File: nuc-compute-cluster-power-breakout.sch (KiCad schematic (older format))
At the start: 20 parts, among them J10 10107844-002LF, J2 BM04B-SRSS-TB-LF-SN, J3 BM04B-SRSS-TB-LF-SN, J5 430450812, J6 430450812, J7 430450812, J8 430450812, J9 430450812, Q11 BC856,215

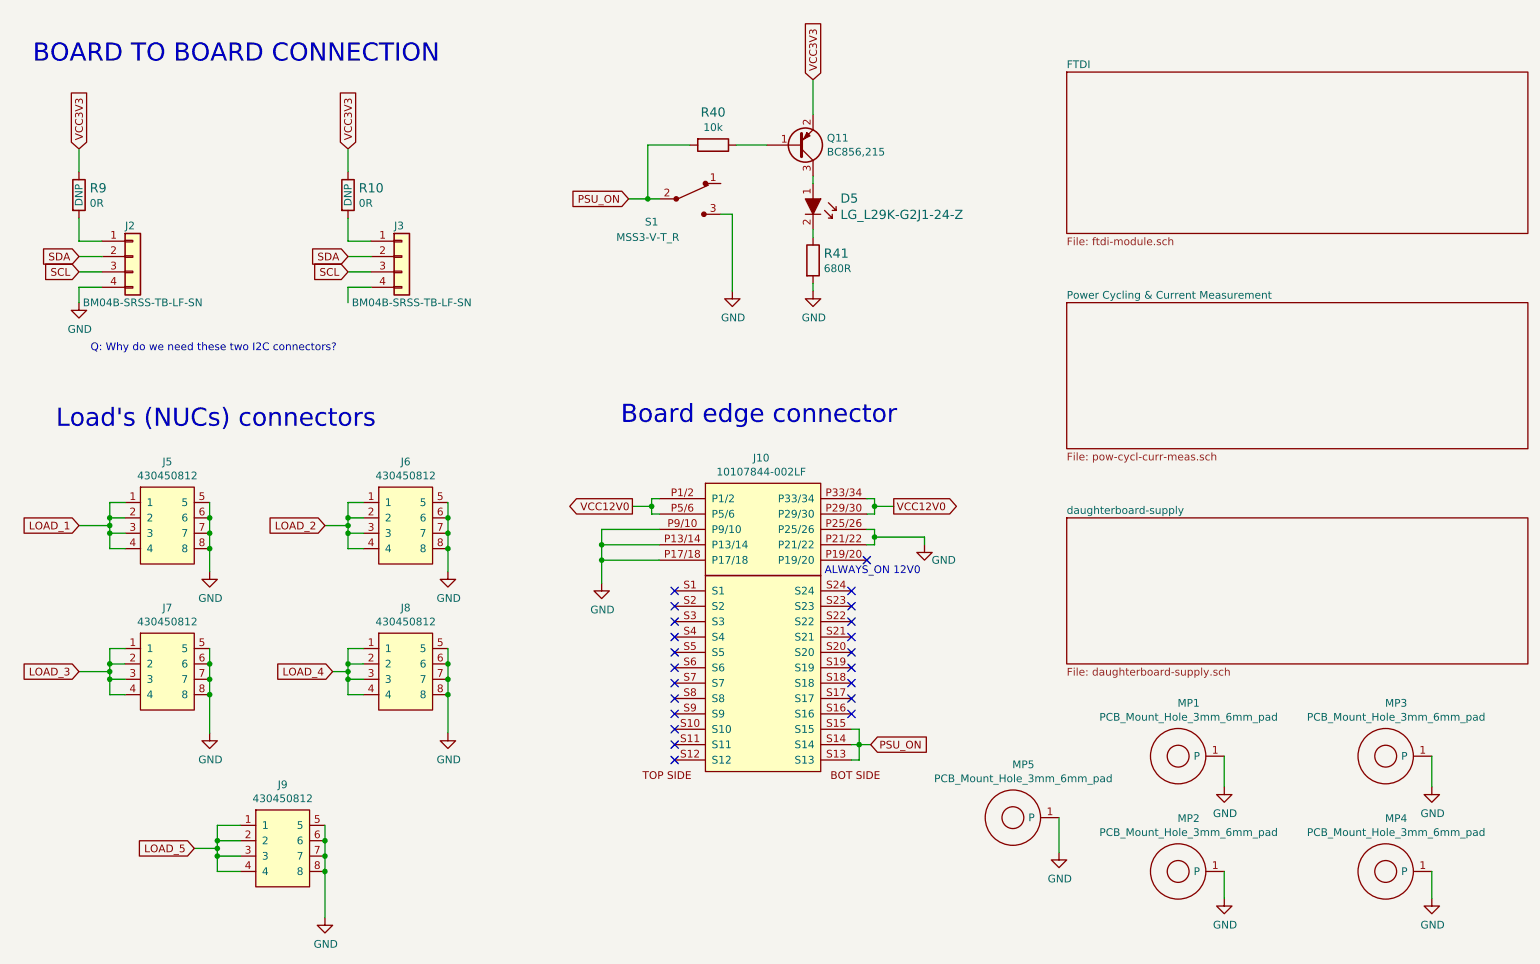
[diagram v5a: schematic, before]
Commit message: Add remarks to the schematic
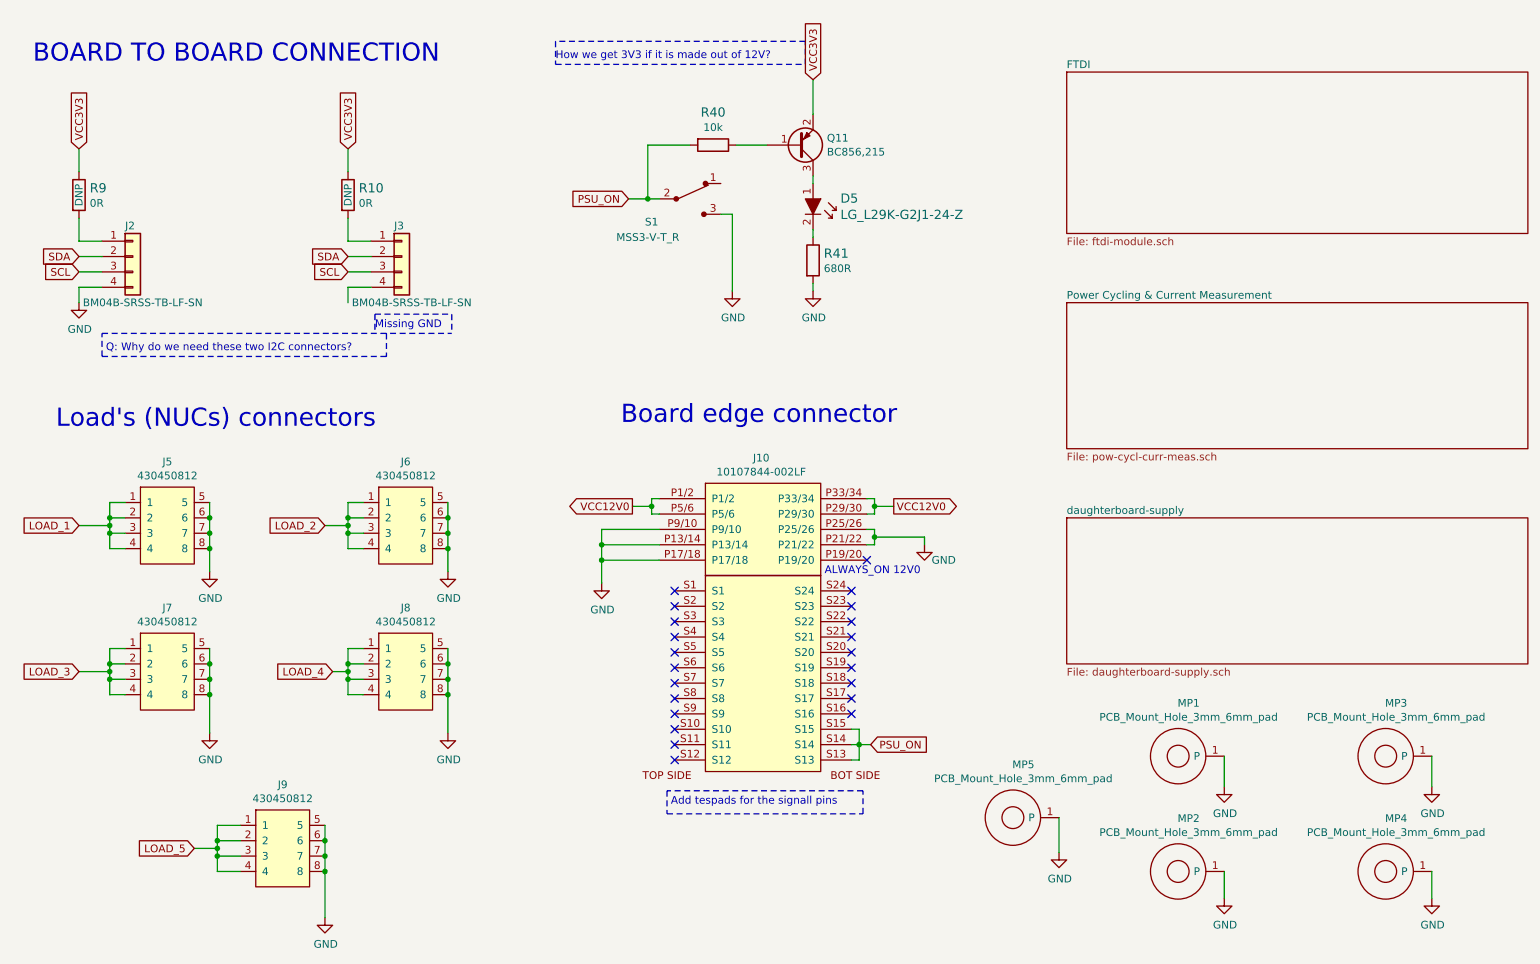
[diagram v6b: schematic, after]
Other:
- note added: "Add tespads for the signall pins"
- note added: "How we get 3V3 if it is made out of 12V?"
- note added: "Missing GND"
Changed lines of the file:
@@
 Wire Wire Line
 	3175 4825 3175 4875
-Text Notes 1500 2750 0    50   ~ 0
+Text Notes 1600 2750 0    50   ~ 0
 Q: Why do we need these two I2C connectors?
 Text Notes 1275 3250 0    118  ~ 0
@@
 Wire Wire Line
 	7800 6000 7800 5775
+Text Notes 3350 2600 0    50   ~ 0
+Missing GND
+Text Notes 4525 850  0    50   ~ 0
+How we get 3V3 if it is made out of 12V?
+Text Notes 5275 5700 0    50   ~ 0
+Add tespads for the signall pins
+Wire Notes Line
+	3425 2625 3425 2775
+Wire Notes Line
+	3425 2775 1575 2775
+Wire Notes Line
+	1575 2775 1575 2625
+Wire Notes Line
+	3350 2500 3850 2500
+Wire Notes Line
+	3850 2500 3850 2625
+Wire Notes Line
+	3350 2500 3350 2625
+Wire Notes Line
+	1575 2625 3850 2625
+Wire Notes Line
+	4525 725  4525 875
+Wire Notes Line
+	4525 875  6150 875
+Wire Notes Line
+	6150 875  6150 725
+Wire Notes Line
+	6150 725  4525 725
+Wire Notes Line
+	5250 5600 5250 5750
+Wire Notes Line
+	5250 5750 6525 5750
+Wire Notes Line
+	6525 5750 6525 5600
+Wire Notes Line
+	6525 5600 5250 5600
 $EndSCHEMATC
